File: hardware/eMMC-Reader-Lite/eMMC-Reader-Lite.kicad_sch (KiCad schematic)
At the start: 35 parts, among them J1 Conn_01x09_Socket, J2 USB_B_Mini, U2 TXS02612, U3 W25X20CLSN, U4 LM1117MP-1.8

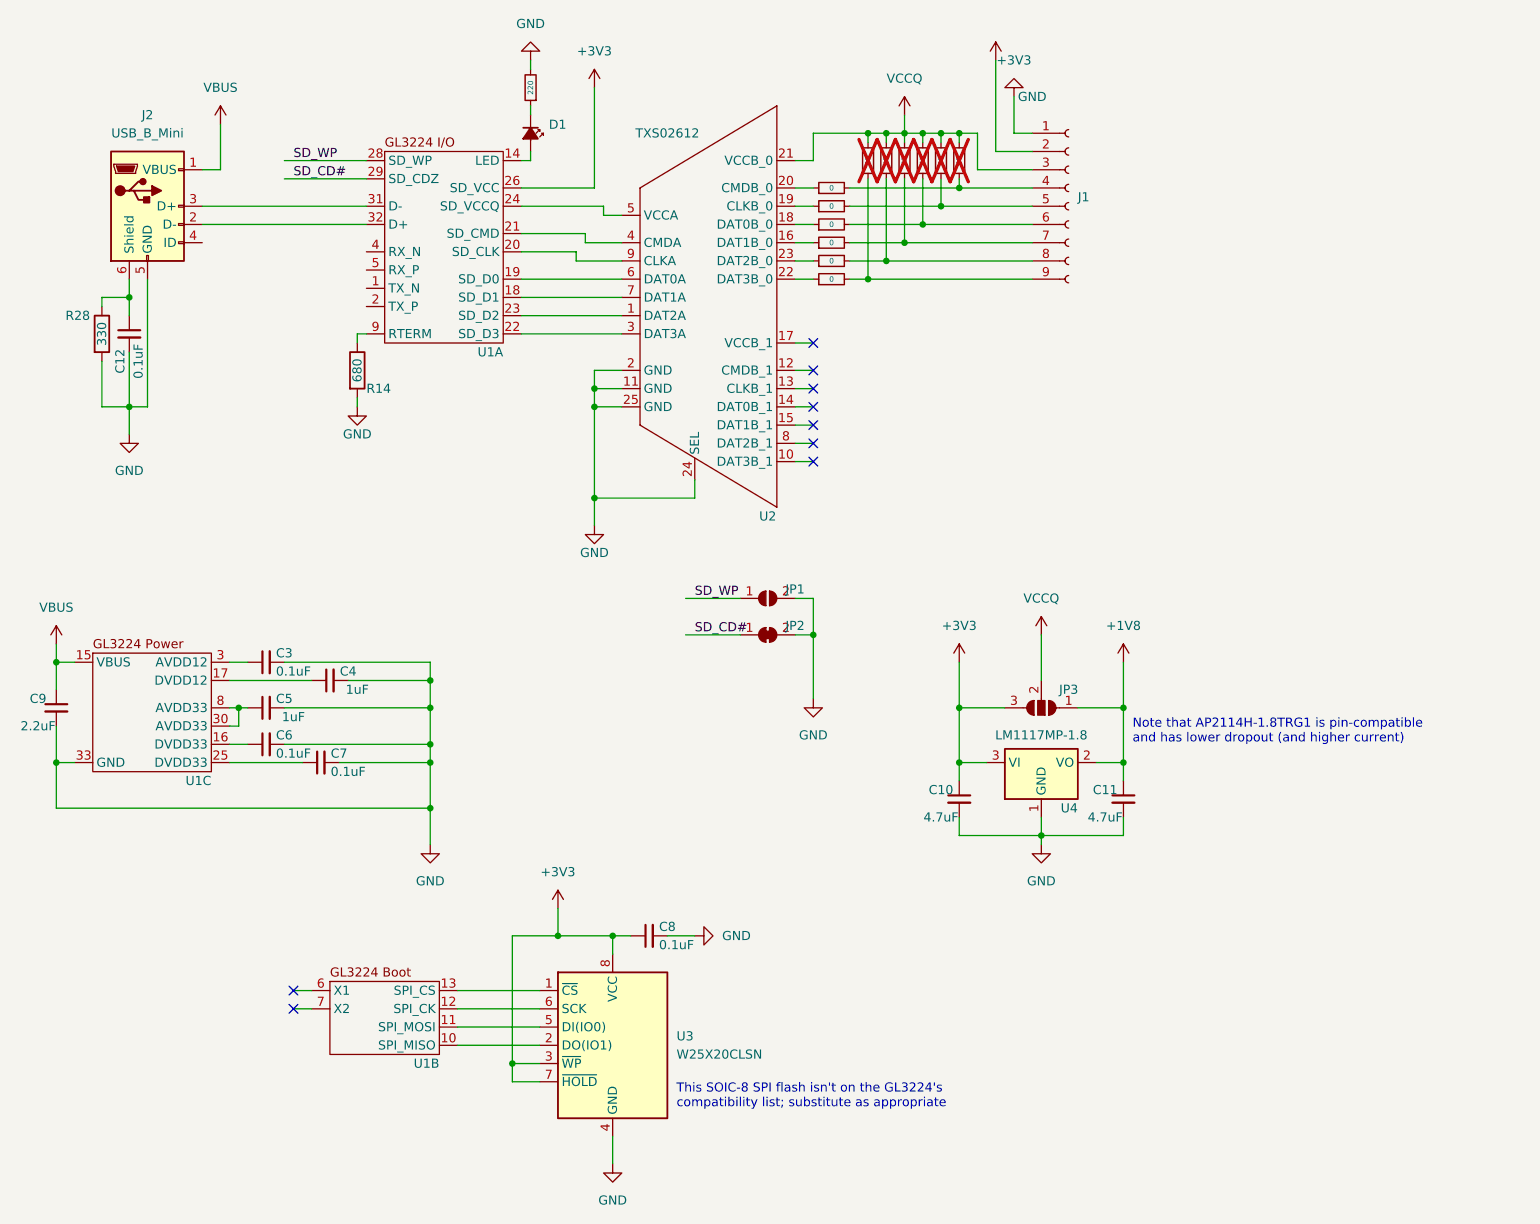
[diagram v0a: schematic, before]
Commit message: Further routing
Need fills, GL3224 test points, length-matching from GL3224

Might need more blinky
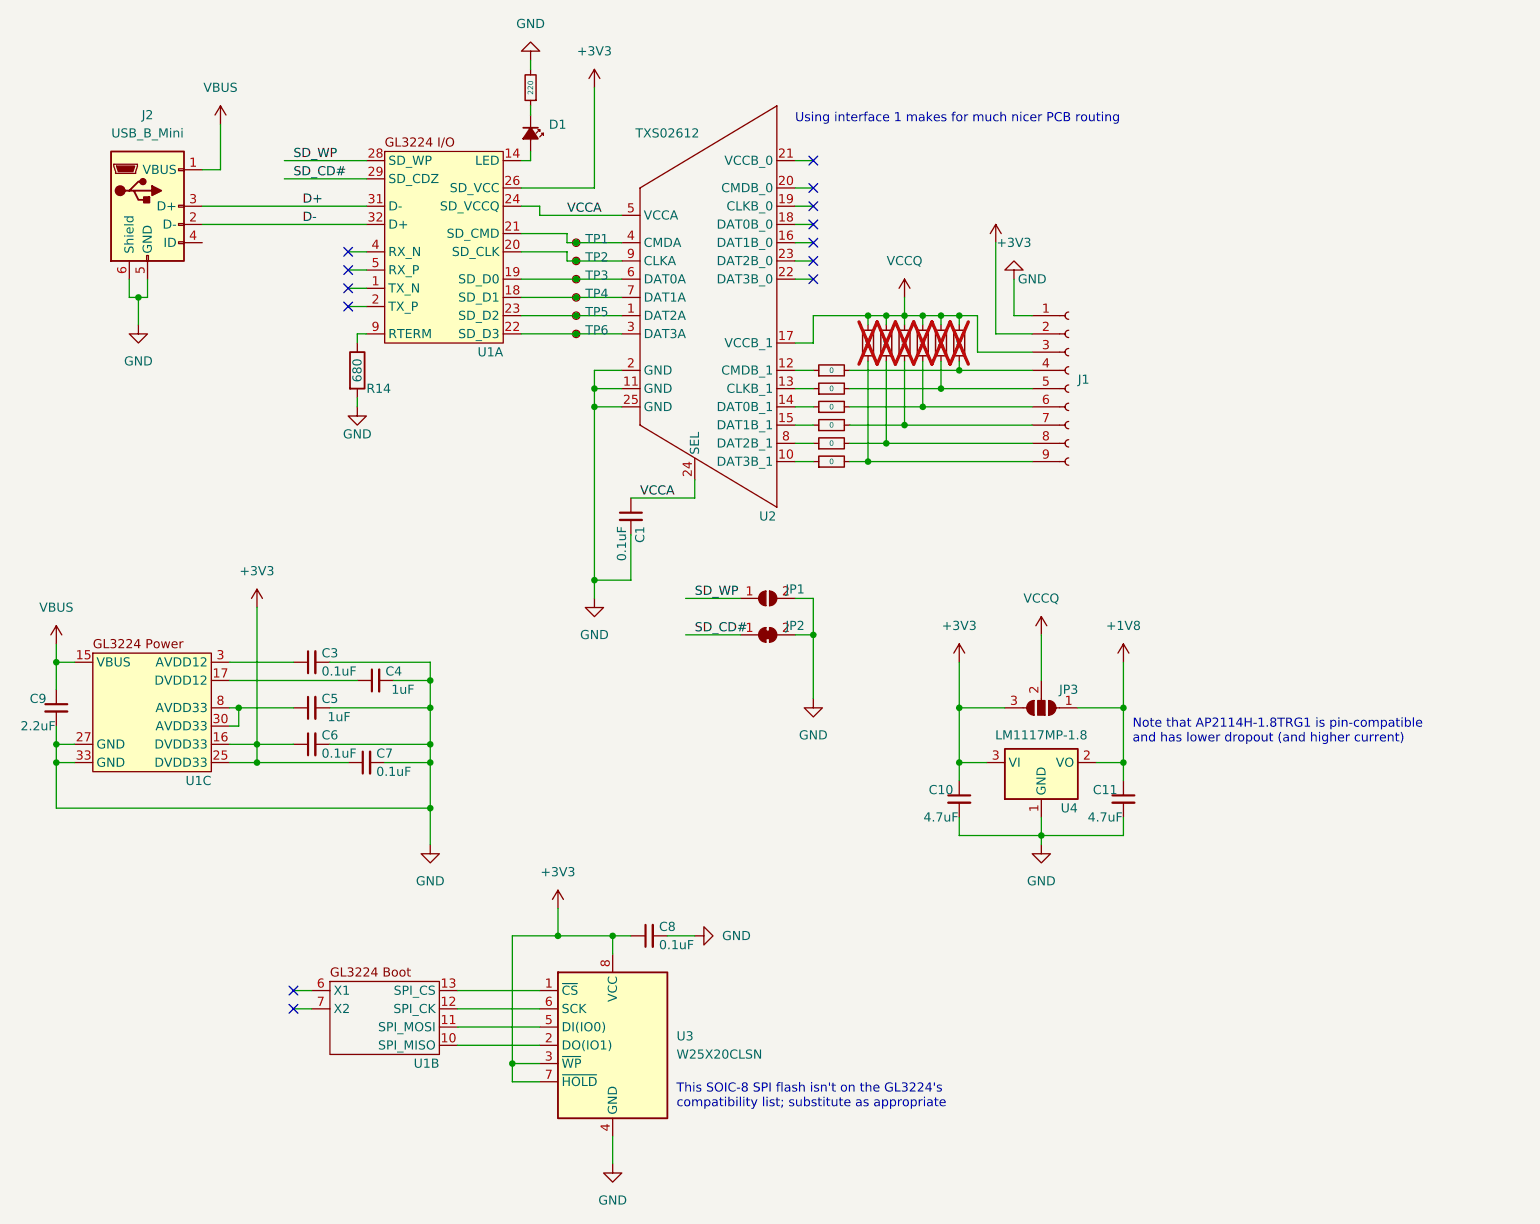
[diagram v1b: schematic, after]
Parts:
- removed C12: 0.1uF, Capacitor_SMD:C_0603_1608Metric_Pad1.08x0.95mm_HandSolder, symbol Device:C_Small
- removed R28: 330, Resistor_SMD:R_0603_1608Metric_Pad0.98x0.95mm_HandSolder, symbol Device:R
- added C1: 0.1uF, Capacitor_SMD:C_0603_1608Metric, symbol Device:C_Small
- added TP1, TP2, TP3, TP4, TP5, TP6: TestPoint_Small, TestPoint:TestPoint_Pad_D1.0mm, symbol Connector:TestPoint_Small
- C10, C11, C3, C4, C5, C6, C7, C8, C9: footprint Capacitor_SMD:C_0603_1608Metric_Pad1.08x0.95mm_HandSolder -> Capacitor_SMD:C_0603_1608Metric
- R1, R10, R11, R12, R13, R14, R2, R3, R4, R5, R6, R7, R8, R9: footprint Resistor_SMD:R_0603_1608Metric_Pad0.98x0.95mm_HandSolder -> Resistor_SMD:R_0603_1608Metric
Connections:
- net +3V3: now also C6.1, C7.1, U1.16 (DVDD33), U1.25 (DVDD33)
- net GND: now also J2.6 (Shield), U1.27 (GND), C1.2; no longer U2.24 (SEL)
- net VCCQ: now also U2.17 (VCCB_1); no longer U2.21 (VCCB_0)
- net at R4.1: now also U2.15 (DAT1B_1); no longer U2.16 (DAT1B_0)
- net at R1.1: now also U2.12 (CMDB_1); no longer U2.20 (CMDB_0)
- net at U1.18 (SD_D1), U2.7 (DAT1A): now also TP4.1
- net at U1.19 (SD_D0), U2.6 (DAT0A): now also TP3.1
- net at U1.20 (SD_CLK), U2.9 (CLKA): now also TP2.1
- net at U1.21 (SD_CMD), U2.4 (CMDA): now also TP1.1
- net at U1.22 (SD_D3), U2.3 (DAT3A): now also TP6.1
- net at U1.23 (SD_D2), U2.1 (DAT2A): now also TP5.1
- net VCCA: now reaches U1.24 (SD_VCCQ), U2.5 (VCCA)
- net VCCA: now also U2.24 (SEL), C1.1
- net D+: now reaches J2.3 (D+), U1.31 (D-)
- net D-: now reaches J2.2 (D-), U1.32 (D+)
- net at R2.1: now also U2.13 (CLKB_1); no longer U2.19 (CLKB_0)
- net at R3.1: now also U2.14 (DAT0B_1); no longer U2.18 (DAT0B_0)
- net at R6.1: now also U2.10 (DAT3B_1); no longer U2.22 (DAT3B_0)
- net at U2.23 (DAT2B_0): no longer R5.1
- net at U2.8 (DAT2B_1): now also R5.1
- no-connect marks 9 -> 13
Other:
- note added: "Using interface 1 makes for much nicer PCB routing"
- moved on the sheet: C3, C4, C5, C6, C7, J1

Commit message: Break out SD_VCC output rail to be distinct from 3V3 net
Add indicator LED for that rail
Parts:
- added D2: LED_Small_Filled, LED_SMD:LED_0603_1608Metric, symbol Device:LED_Small_Filled
- added R15: 220, Resistor_SMD:R_0603_1608Metric, symbol Device:R_Small
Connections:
- net +3V3: no longer C10.1, J1.2 (Pin_2), JP3.3 (B), U1.26 (SD_VCC), U4.3 (VI)
- net GND: now also R15.2
- new net: D2.1 (K), R15.1
- new net SD_VCC: C10.1, D2.2 (A), J1.2 (Pin_2), JP3.3 (B), U1.26 (SD_VCC), U4.3 (VI)
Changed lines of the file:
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@@
   (junction (at 49.53 118.11) (diameter 0) (color 0 0 0 0)
+  )
+  (junction (at 96.52 25.4) (diameter 0) (color 0 0 0 0)
   )
   (junction (at 73.66 124.46) (diameter 0) (color 0 0 0 0)
@@
     (stroke (width 0) (type default))
   )
+  (wire (pts (xy 146.05 45.72) (xy 152.4 45.72))
+    (stroke (width 0) (type default))
+  )
   (wire (pts (xy 73.66 104.14) (xy 73.66 106.68))
     (stroke (width 0) (type default))
@@
     (stroke (width 0) (type default))
   )
+  (wire (pts (xy 138.43 104.14) (xy 147.32 104.14))
+    (stroke (width 0) (type default))
+  )
   (wire (pts (xy 124.46 59.69) (xy 127 59.69))
     (stroke (width 0) (type default))
@@
     (stroke (width 0) (type default))
   )
+  (wire (pts (xy 96.52 25.4) (xy 96.52 38.1))
+    (stroke (width 0) (type default))
+  )
   (wire (pts (xy 124.46 48.26) (xy 127 48.26))
     (stroke (width 0) (type default))
@@
     (stroke (width 0) (type default))
   )
+  (wire (pts (xy 96.52 17.78) (xy 106.68 17.78))
+    (stroke (width 0) (type default))
+  )
   (wire (pts (xy 54.61 152.4) (xy 57.15 152.4))
     (stroke (width 0) (type default))
@@
     (stroke (width 0) (type default))
   )
+  (wire (pts (xy 101.6 25.4) (xy 102.87 25.4))
+    (stroke (width 0) (type default))
+  )
   (wire (pts (xy 96.52 92.71) (xy 96.52 95.25))
     (stroke (width 0) (type default))
@@
     (stroke (width 0) (type default))
   )
-  (wire (pts (xy 96.52 24.13) (xy 96.52 38.1))
+  (wire (pts (xy 96.52 17.78) (xy 96.52 25.4))
     (stroke (width 0) (type default))
   )
@@
   )
   (wire (pts (xy 149.86 60.96) (xy 157.48 60.96))
+    (stroke (width 0) (type default))
+  )
+  (wire (pts (xy 109.22 25.4) (xy 107.95 25.4))
     (stroke (width 0) (type default))
   )
@@
     (effects (font (size 1.27 1.27)) (justify left bottom))
   )
+  (label "SD_VCC" (at 146.05 45.72 0) (fields_autoplaced)
+    (effects (font (size 1.27 1.27)) (justify left bottom))
+  )
   (label "SD_CD#" (at 54.61 36.83 0) (fields_autoplaced)
     (effects (font (size 1.27 1.27)) (justify left bottom))
   )
+  (label "SD_VCC" (at 139.7 104.14 0) (fields_autoplaced)
+    (effects (font (size 1.27 1.27)) (justify left bottom))
+  )
   (label "SD_CD#" (at 110.49 100.33 0) (fields_autoplaced)
     (effects (font (size 1.27 1.27)) (justify left bottom))
@@
     (effects (font (size 1.27 1.27)) (justify left bottom))
   )
+  (label "SD_VCC" (at 99.06 17.78 0) (fields_autoplaced)
+    (effects (font (size 1.27 1.27)) (justify left bottom))
+  )
   (label "SD_WP" (at 54.61 34.29 0) (fields_autoplaced)
     (effects (font (size 1.27 1.27)) (justify left bottom))
@@
         (path "/f3b19d86-7061-4f69-a0e8-c16fd2b5fe18"
           (reference "R4") (unit 1)
+        )
+      )
+    )
+  )
+  (symbol (lib_id "Device:LED_Small_Filled") (at 99.06 25.4 180) (unit 1)
+    (in_bom yes) (on_board yes) (dnp no) (fields_autoplaced)
+    (property "Reference" "D2" (at 100.2665 27.94 90)
+      (effects (font (size 1.27 1.27)) (justify left))
+    )
+    (property "Value" "LED_Small_Filled" (at 97.7265 27.94 90)
+      (effects (font (size 1.27 1.27)) (justify left) hide)
+    )
+    (property "Footprint" "LED_SMD:LED_0603_1608Metric" (at 99.06 25.4 90)
+      (effects (font (size 1.27 1.27)) hide)
+    )
+    (property "Datasheet" "~" (at 99.06 25.4 90)
+      (effects (font (size 1.27 1.27)) hide)
+    )
+    (pin "1")
+    (pin "2")
+    (instances
+      (project "eMMC-Reader-Lite"
+        (path "/f3b19d86-7061-4f69-a0e8-c16fd2b5fe18"
+          (reference "D2") (unit 1)
         )
       )
@@
     )
   )
+  (symbol (lib_id "power:GND") (at 109.22 25.4 90) (unit 1)
+    (in_bom yes) (on_board yes) (dnp no) (fields_autoplaced)
+    (property "Reference" "#PWR021" (at 115.57 25.4 0)
+      (effects (font (size 1.27 1.27)) hide)
+    )
+    (property "Value" "GND" (at 114.3 25.4 0)
+      (effects (font (size 1.27 1.27)))
+    )
+    (property "Footprint" "" (at 109.22 25.4 0)
+      (effects (font (size 1.27 1.27)) hide)
+    )
+    (property "Datasheet" "" (at 109.22 25.4 0)
+      (effects (font (size 1.27 1.27)) hide)
+    )
+    (pin "1")
+    (instances
+      (project "eMMC-Reader-Lite"
+        (path "/f3b19d86-7061-4f69-a0e8-c16fd2b5fe18"
+          (reference "#PWR021") (unit 1)
+        )
+      )
+    )
+  )
   (symbol (lib_id "Device:C_Small") (at 57.15 110.49 90) (unit 1)
     (in_bom yes) (on_board yes) (dnp no)
@@
         (path "/f3b19d86-7061-4f69-a0e8-c16fd2b5fe18"
           (reference "#PWR08") (unit 1)
-        )
-      )
-    )
-  )
-  (symbol (lib_id "power:+3V3") (at 152.4 45.72 0) (unit 1)
-    (in_bom yes) (on_board yes) (dnp no)
-    (property "Reference" "#PWR07" (at 152.4 49.53 0)
-      (effects (font (size 1.27 1.27)) hide)
-    )
-    (property "Value" "+3V3" (at 154.94 45.72 0)
-      (effects (font (size 1.27 1.27)))
-    )
-    (property "Footprint" "" (at 152.4 45.72 0)
-      (effects (font (size 1.27 1.27)) hide)
-    )
-    (property "Datasheet" "" (at 152.4 45.72 0)
-      (effects (font (size 1.27 1.27)) hide)
-    )
-    (pin "1")
-    (instances
-      (project "eMMC-Reader-Lite"
-        (path "/f3b19d86-7061-4f69-a0e8-c16fd2b5fe18"
-          (reference "#PWR07") (unit 1)
         )
       )
@@
     )
   )
+  (symbol (lib_id "Device:R_Small") (at 105.41 25.4 90) (unit 1)
+    (in_bom yes) (on_board yes) (dnp no)
+    (property "Reference" "R15" (at 105.41 20.32 90)
+      (effects (font (size 1.27 1.27)) hide)
+    )
+    (property "Value" "220" (at 105.41 25.4 90)
+      (effects (font (size 0.762 0.762)))
+    )
+    (property "Footprint" "Resistor_SMD:R_0603_1608Metric" (at 105.41 25.4 0)
+      (effects (font (size 1.27 1.27)) hide)
+    )
+    (property "Datasheet" "~" (at 105.41 25.4 0)
+      (effects (font (size 1.27 1.27)) hide)
+    )
+    (pin "1")
+    (pin "2")
+    (instances
+      (project "eMMC-Reader-Lite"
+        (path "/f3b19d86-7061-4f69-a0e8-c16fd2b5fe18"
+          (reference "R15") (unit 1)
+        )
+      )
+    )
+  )
   (symbol (lib_id "Device:C_Small") (at 57.15 104.14 90) (unit 1)
     (in_bom yes) (on_board yes) (dnp no)
@@
     )
   )
-  (symbol (lib_id "power:+3V3") (at 147.32 104.14 0) (unit 1)
-    (in_bom yes) (on_board yes) (dnp no) (fields_autoplaced)
-    (property "Reference" "#PWR09" (at 147.32 107.95 0)
-      (effects (font (size 1.27 1.27)) hide)
-    )
-    (property "Value" "+3V3" (at 147.32 99.06 0)
-      (effects (font (size 1.27 1.27)))
-    )
-    (property "Footprint" "" (at 147.32 104.14 0)
-      (effects (font (size 1.27 1.27)) hide)
-    )
-    (property "Datasheet" "" (at 147.32 104.14 0)
-      (effects (font (size 1.27 1.27)) hide)
-    )
-    (pin "1")
-    (instances
-      (project "eMMC-Reader-Lite"
-        (path "/f3b19d86-7061-4f69-a0e8-c16fd2b5fe18"
-          (reference "#PWR09") (unit 1)
-        )
-      )
-    )
-  )
   (symbol (lib_id "Device:R_Small") (at 139.7 59.69 180) (unit 1)
     (in_bom no) (on_board yes) (dnp yes)
@@
         )
       )
-    )
-  )
-  (symbol (lib_id "power:+3V3") (at 96.52 24.13 0) (unit 1)
-    (in_bom yes) (on_board yes) (dnp no) (fields_autoplaced)
-    (property "Reference" "#PWR06" (at 96.52 27.94 0)
-      (effects (font (size 1.27 1.27)) hide)
-    )
-    (property "Value" "+3V3" (at 96.52 19.05 0)
-      (effects (font (size 1.27 1.27)))
-    )
-    (property "Footprint" "" (at 96.52 24.13 0)
-      (effects (font (size 1.27 1.27)) hide)
-    )
-    (property "Datasheet" "" (at 96.52 24.13 0)
-      (effects (font (size 1.27 1.27)) hide)
-    )
-    (pin "1")
-    (instances
-      (project "eMMC-Reader-Lite"
-        (path "/f3b19d86-7061-4f69-a0e8-c16fd2b5fe18"
-          (reference "#PWR06") (unit 1)
-        )
-      )

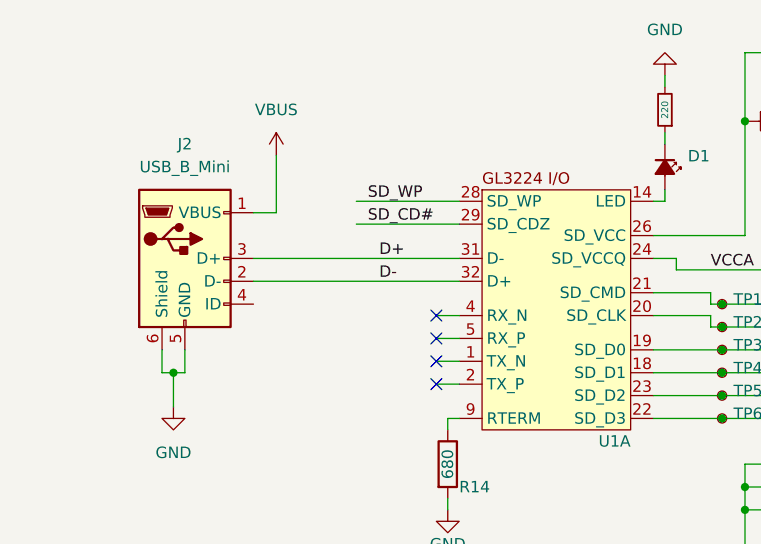
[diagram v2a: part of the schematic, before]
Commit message: Fix swapped USB data lines
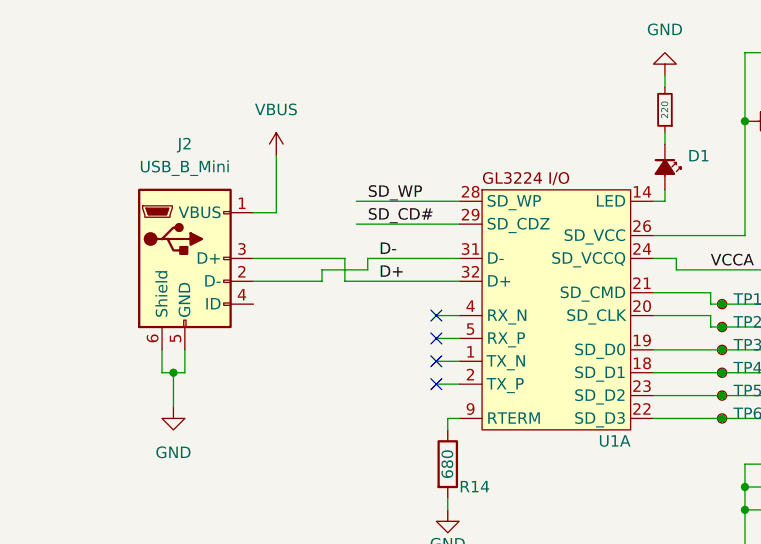
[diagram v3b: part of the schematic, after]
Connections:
- net D+: now also U1.32 (D+); no longer U1.31 (D-)
- net D-: now also U1.31 (D-); no longer U1.32 (D+)
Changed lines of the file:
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@@
+    (stroke (width 0) (type default))
+  )
+  (wire (pts (xy 49.53 43.18) (xy 41.91 43.18))
     (stroke (width 0) (type default))
   )
@@
     (stroke (width 0) (type default))
   )
+  (wire (pts (xy 52.07 43.18) (xy 64.77 43.18))
+    (stroke (width 0) (type default))
+  )
   (wire (pts (xy 21.59 104.14) (xy 24.13 104.14))
     (stroke (width 0) (type default))
@@
     (stroke (width 0) (type default))
   )
+  (wire (pts (xy 41.91 40.64) (xy 52.07 40.64))
+    (stroke (width 0) (type default))
+  )
   (wire (pts (xy 139.7 62.23) (xy 139.7 71.12))
     (stroke (width 0) (type default))
@@
     (stroke (width 0) (type default))
   )
+  (wire (pts (xy 64.77 40.64) (xy 54.61 40.64))
+    (stroke (width 0) (type default))
+  )
   (wire (pts (xy 73.66 124.46) (xy 73.66 129.54))
     (stroke (width 0) (type default))
@@
     (stroke (width 0) (type default))
   )
-  (wire (pts (xy 41.91 40.64) (xy 64.77 40.64))
-    (stroke (width 0) (type default))
-  )
   (wire (pts (xy 147.32 63.5) (xy 157.48 63.5))
     (stroke (width 0) (type default))
@@
     (stroke (width 0) (type default))
   )
+  (wire (pts (xy 54.61 41.91) (xy 49.53 41.91))
+    (stroke (width 0) (type default))
+  )
   (wire (pts (xy 158.75 125.73) (xy 158.75 128.27))
     (stroke (width 0) (type default))
@@
     (stroke (width 0) (type default))
   )
+  (wire (pts (xy 54.61 40.64) (xy 54.61 41.91))
+    (stroke (width 0) (type default))
+  )
   (wire (pts (xy 92.71 45.72) (xy 92.71 44.45))
     (stroke (width 0) (type default))
@@
     (stroke (width 0) (type default))
   )
+  (wire (pts (xy 52.07 40.64) (xy 52.07 43.18))
+    (stroke (width 0) (type default))
+  )
   (wire (pts (xy 92.71 46.99) (xy 92.71 48.26))
     (stroke (width 0) (type default))
   )
+  (wire (pts (xy 49.53 41.91) (xy 49.53 43.18))
+    (stroke (width 0) (type default))
+  )
   (wire (pts (xy 137.16 55.88) (xy 137.16 57.15))
     (stroke (width 0) (type default))
@@
   )
   (wire (pts (xy 34.29 50.8) (xy 34.29 53.34))
-    (stroke (width 0) (type default))
-  )
-  (wire (pts (xy 41.91 43.18) (xy 64.77 43.18))
     (stroke (width 0) (type default))
   )
@@
     (effects (font (size 1.27 1.27)) (justify left bottom))
   )
-  (label "D-" (at 55.88 43.18 0) (fields_autoplaced)
-    (effects (font (size 1.27 1.27)) (justify left bottom))
-  )
-  (label "D+" (at 55.88 40.64 0) (fields_autoplaced)
-    (effects (font (size 1.27 1.27)) (justify left bottom))
-  )
+  (label "D-" (at 55.88 40.64 0) (fields_autoplaced)
+    (effects (font (size 1.27 1.27)) (justify left bottom))
+  )
+  (label "D+" (at 55.88 43.18 0) (fields_autoplaced)
+    (effects (font (size 1.27 1.27)) (justify left bottom))
+  )
